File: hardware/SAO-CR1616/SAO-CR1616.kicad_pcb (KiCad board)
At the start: 2 copper layers, 44 x 29.7 mm, 39 parts, among them J2 SAO v1.69bis addon, J3 SAO v1.69bis badge, P1 Conn_01x02, P2 Conn_01x02, P3 Conn_01x02, P4 Conn_01x02, P5 Conn_01x02, P6 Conn_01x02

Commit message: cleanup fab files
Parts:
- removed ? (x20): , 
- removed BC1, BC2, BC3, BC4, BC5, BC6, BC7: 1u, Capacitor_SMD:C_0805_2012Metric_Pad1.18x1.45mm_HandSolder
- removed J3: SAO v1.69bis badge, Connector_IDC:IDC-Header_2x03_P2.54mm_Vertical
- removed P1, P2, P3, P4, P5, P6: Conn_01x02, Connector_PinHeader_2.54mm:PinHeader_1x02_P2.54mm_Vertical
- moved B3 28.7 mm to (100.0, 150.0)
- moved B4 28.7 mm to (100.0, 150.0)
- moved SAO-P1 28.7 mm to (100.0, 150.0)
- moved SAO-P2 28.7 mm to (100.0, 150.0)
- moved J2 28.7 mm to (97.5, 165.1)
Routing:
- net +3V0: track 43.1 -> 16.2 mm
- net GND: track 49.3 -> 22.5 mm
- removed copper zone on F.Cu, net +3V0
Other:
- board size 44 x 29.7 mm -> 16 x 29.5 mm
- board text removed: "JLCJLCJLCJLC"
- board text removed: "import QR SVG scale 0.2"

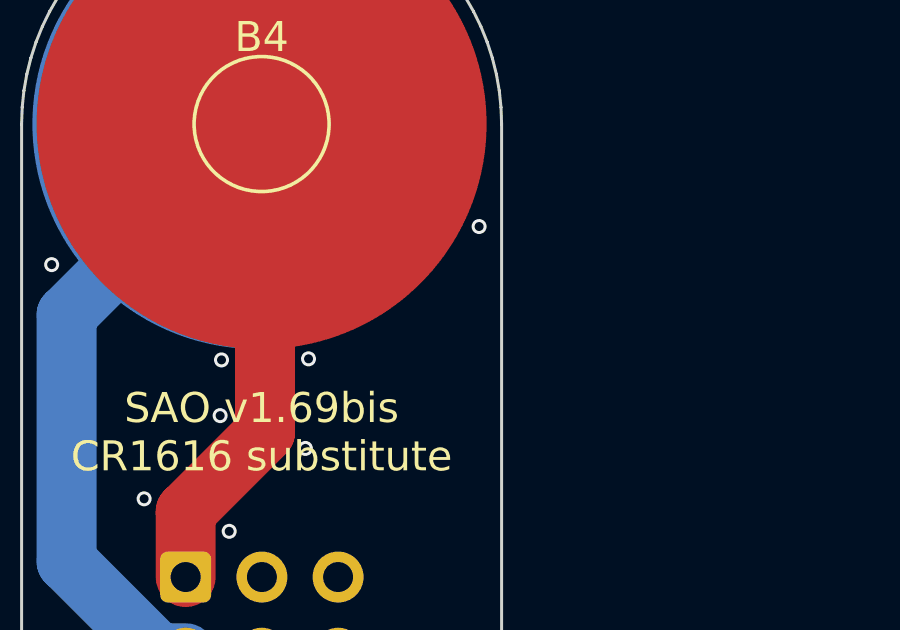
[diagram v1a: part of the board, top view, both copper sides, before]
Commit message: add polarity indicators
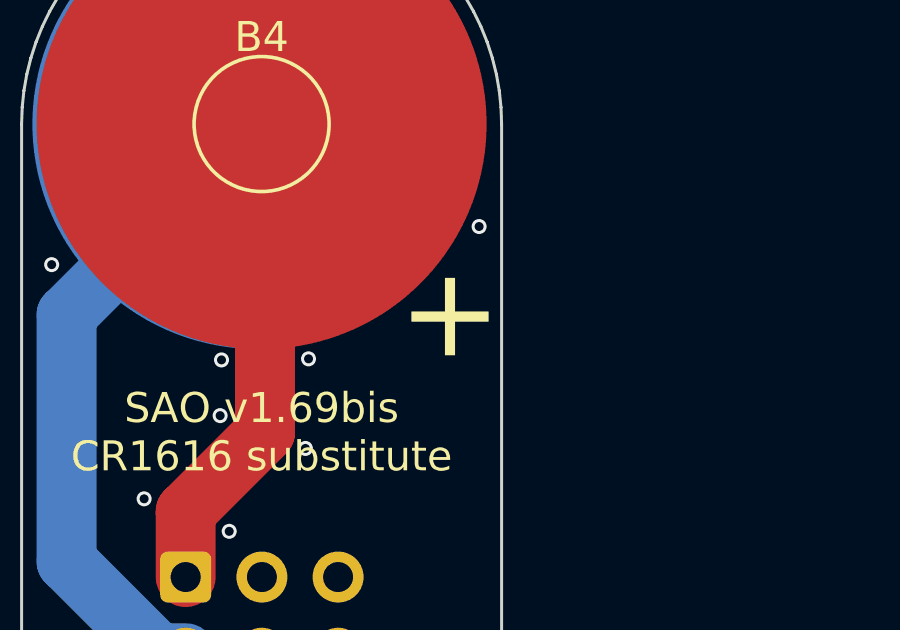
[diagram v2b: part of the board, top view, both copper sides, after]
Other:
- board text added: "+"
- board text added: "-"
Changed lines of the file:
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@@
+		)
+	)
+	(gr_text "+"
+		(at 106.28 156.32 0)
+		(layer "F.SilkS")
+		(effects
+			(font
+				(size 3 3)
+				(thickness 0.2)
+			)
+		)
+	)
+	(gr_text "-"
+		(at 106.28 156.35 0)
+		(layer "B.SilkS")
+		(effects
+			(font
+				(size 3 3)
+				(thickness 0.2)
+			)
 		)
 	)

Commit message: prep for another fab run
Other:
- board text removed: "+"
- board text removed: "-"
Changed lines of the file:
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@@
 	(net 6 "unconnected-(J2-GPIO2-Pad6)")
 	(footprint "TestPoint:TestPoint_Pad_D4.0mm"
-		(locked yes)
 		(layer "F.Cu")
 		(at 100 150)
@@
 	)
 	(footprint ""
-		(locked yes)
 		(layer "B.Cu")
 		(at 100 150 180)
@@
 	)
 	(footprint ""
-		(locked yes)
 		(layer "B.Cu")
 		(at 100 150 180)
@@
 	)
 	(footprint "Connector_IDC:IDC-Header_2x03_P2.54mm_Vertical"
-		(locked yes)
 		(layer "B.Cu")
 		(at 97.47 165.1 -90)
@@
 	)
 	(footprint "TestPoint:TestPoint_Pad_D4.0mm"
-		(locked yes)
 		(layer "B.Cu")
 		(at 100 150 180)
@@
 		)
 		(fill no)
-		(locked yes)
 		(layer "Edge.Cuts")
 	)
 	(gr_text "SAO v1.69bis\nCR1616 substitute"
-		(locked yes)
 		(at 100 160.274 0)
 		(layer "F.SilkS")
@@
 		)
 	)
-	(gr_text "+"
-		(at 106.28 156.32 0)
-		(layer "F.SilkS")
-		(effects
-			(font
-				(size 3 3)
-				(thickness 0.2)
-			)
-		)
-	)
-	(gr_text "-"
-		(at 106.28 156.35 0)
-		(layer "B.SilkS")
-		(effects
-			(font
-				(size 3 3)
-				(thickness 0.2)
-			)
-		)
-	)
 	(via
 		(at 96.083863 162.492411)
@@
 		(drill 0.3)
 		(layers "F.Cu" "B.Cu")
-		(locked yes)
 		(free yes)
 		(net 1)
@@
 		(drill 0.3)
 		(layers "F.Cu" "B.Cu")
-		(locked yes)
 		(free yes)
 		(net 1)
@@
 		(drill 0.3)
 		(layers "F.Cu" "B.Cu")
-		(locked yes)
 		(free yes)
 		(net 1)
@@
 		(drill 0.3)
 		(layers "F.Cu" "B.Cu")
-		(locked yes)
 		(free yes)
 		(net 1)
@@
 		(drill 0.3)
 		(layers "F.Cu" "B.Cu")
-		(locked yes)
 		(free yes)
 		(net 1)
@@
 		(drill 0.3)
 		(layers "F.Cu" "B.Cu")
-		(locked yes)
 		(free yes)
 		(net 1)
@@
 		(drill 0.3)
 		(layers "F.Cu" "B.Cu")
-		(locked yes)
 		(free yes)
 		(net 1)
@@
 		(drill 0.3)
 		(layers "F.Cu" "B.Cu")
-		(locked yes)
 		(net 1)
 	)
@@
 		(drill 0.3)
 		(layers "F.Cu" "B.Cu")
-		(locked yes)
 		(free yes)
 		(net 1)
@@
 		(drill 0.3)
 		(layers "F.Cu" "B.Cu")
-		(locked yes)
 		(free yes)
 		(net 1)
@@
 		(end 99.86 150)
 		(width 2)
-		(locked yes)
 		(layer "B.Cu")
 		(net 1)
@@
 		(end 93.5 156.36)
 		(width 2)
-		(locked yes)
 		(layer "B.Cu")
 		(net 1)
@@
 		(end 96.558 167.64)
 		(width 2)
-		(locked yes)
 		(layer "B.Cu")
 		(net 1)
@@
 		(end 93.5 164.582)
 		(width 2)
-		(locked yes)
 		(layer "B.Cu")
 		(net 1)
@@
 		(end 100.114 150.114)
 		(width 2)
-		(locked yes)
 		(layer "F.Cu")
 		(net 2)
@@
 		(end 100 150)
 		(width 2)
-		(locked yes)
 		(layer "F.Cu")
 		(net 2)
@@
 		(end 97.47 162.918)
 		(width 2)
-		(locked yes)
 		(layer "F.Cu")
 		(net 2)
@@
 		(end 100.114 160.274)
 		(width 2)
-		(locked yes)
 		(layer "F.Cu")
 		(net 2)
@@
 		(net 1)
 		(net_name "GND")
-		(locked yes)
 		(layers "F.Cu" "B.Cu")
 		(hatch edge 0.5)
